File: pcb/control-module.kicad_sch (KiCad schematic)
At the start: 27 parts, among them J1 Screw_Terminal_01x06, J2 Conn_01x07_Pin, SW1 SW_DIP_x04, U1 TPS2116DRL

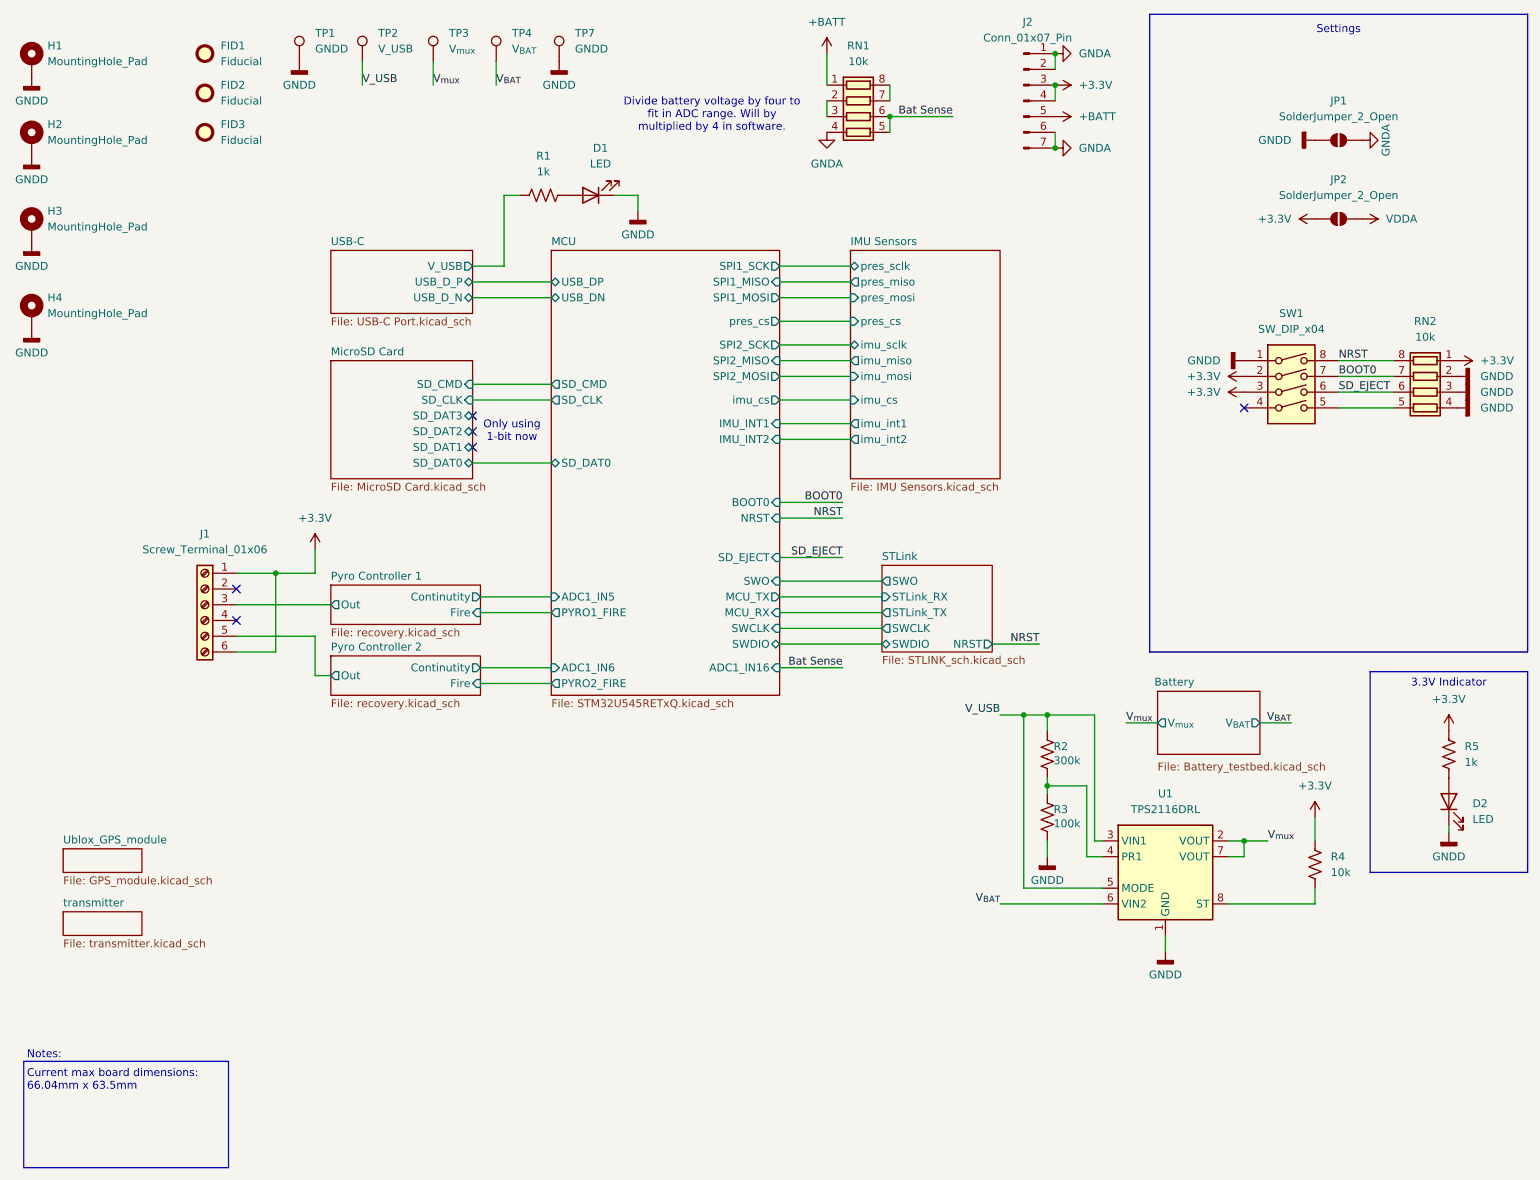
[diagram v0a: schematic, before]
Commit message: Updated Board size and layout
Full Layout of Rev 2 board, without RF shield and other updates.
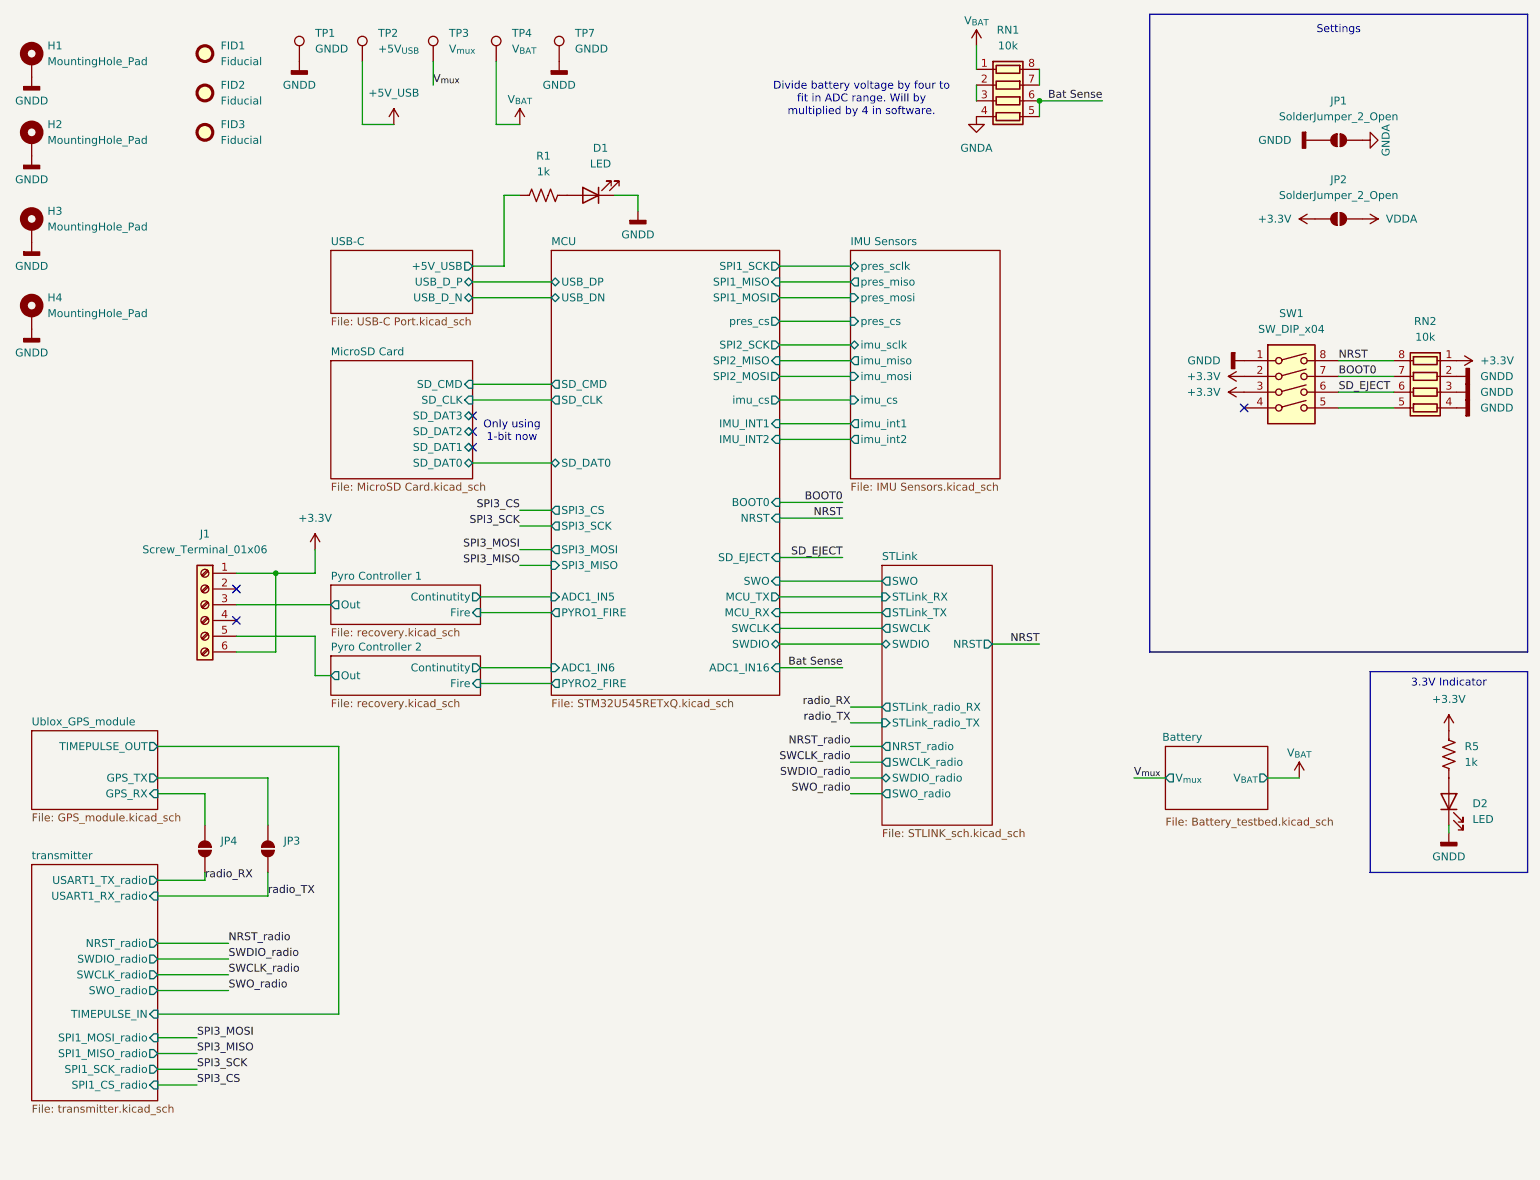
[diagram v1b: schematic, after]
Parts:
- removed J2: Conn_01x07_Pin, Connector_PinHeader_2.54mm:PinHeader_1x07_P2.54mm_Vertical, symbol Connector:Conn_01x07_Pin
- removed R2: 300k, Resistor_SMD:R_0603_1608Metric_Pad0.98x0.95mm_HandSolder, symbol Device:R_US
- removed R3: 100k, Resistor_SMD:R_0603_1608Metric_Pad0.98x0.95mm_HandSolder, symbol Device:R_US
- removed R4: 10k, Resistor_SMD:R_0603_1608Metric, symbol Device:R_US
- removed U1: TPS2116DRL, Package_TO_SOT_SMD:SOT-583-8, symbol Power_Management:TPS2116DRL
- added JP3, JP4: SolderJumper_2_Open, Jumper:SolderJumper-2_P1.3mm_Open_RoundedPad1.0x1.5mm, symbol Jumper:SolderJumper_2_Open
- TP2: value V_USB -> +5V_{USB}
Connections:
- net +BATT is gone; now on net V_{BAT}: RN1.1 (R1.1)
- net USB-C/V_USB renamed USB-C/+5V_USB
- net V_USB renamed +5V_USB
- new net Ublox_GPS_module/GPS_RX: JP4.2 (B)
- new net Ublox_GPS_module/GPS_TX: JP3.1 (A)
- new net radio_RX: JP4.1 (A)
- new net radio_TX: JP3.2 (B)
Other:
- sheet MCU ports: added SPI3_CS, SPI3_MISO, SPI3_MOSI, SPI3_SCK; removed none
- sheet STLink ports: added NRST_radio, STLink_radio_RX, STLink_radio_TX, SWCLK_radio, SWDIO_radio, SWO_radio; removed none
- sheet USB-C ports: added +5V_USB; removed V_USB
- sheet Ublox_GPS_module ports: added GPS_RX, GPS_TX, TIMEPULSE_OUT; removed none
- sheet transmitter ports: added NRST_radio, SPI1_CS_radio, SPI1_MISO_radio, SPI1_MOSI_radio, SPI1_SCK_radio, SWCLK_radio, SWDIO_radio, SWO_radio, TIMEPULSE_IN, USART1_RX_radio, USART1_TX_radio; removed none
- note removed: "Current max board dimensions: 66.04mm x 63.5mm"
- note removed: "Notes:"
- moved on the sheet: RN1
